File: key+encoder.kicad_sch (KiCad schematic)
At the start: 2 parts, among them SW10 SW_Push

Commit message: routing improvements
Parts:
- renumbered EN7 to EN5, SW10 to SW7
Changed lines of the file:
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@@
   (symbol (lib_id "Device:RotaryEncoder_Switch") (at 143.51 121.92 0) (mirror y)
     (in_bom yes) (on_board yes) (fields_autoplaced)
-    (property "Reference" "EN7" (id 0) (at 143.51 111.76 0))
+    (property "Reference" "EN5" (id 0) (at 143.51 111.76 0))
     (property "Value" "RotaryEncoder_Switch" (id 1) (at 143.51 114.3 0))
     (property "Footprint" "Keeby-Cat Footprints:RotaryEncoder_Alps_EC11E-Switch_Vertical_H20mm_nomount_alt" (id 2) (at 147.32 117.856 0)
@@
   (symbol (lib_id "Switch:SW_Push") (at 140.97 96.52 0)
     (in_bom yes) (on_board yes) (fields_autoplaced)
-    (property "Reference" "SW10" (id 0) (at 140.97 88.9 0))
+    (property "Reference" "SW7" (id 0) (at 140.97 88.9 0))
     (property "Value" "SW_Push" (id 1) (at 140.97 91.44 0))
     (property "Footprint" "kbd-footprints:CherryMX_1u_north" (id 2) (at 140.97 91.44 0)

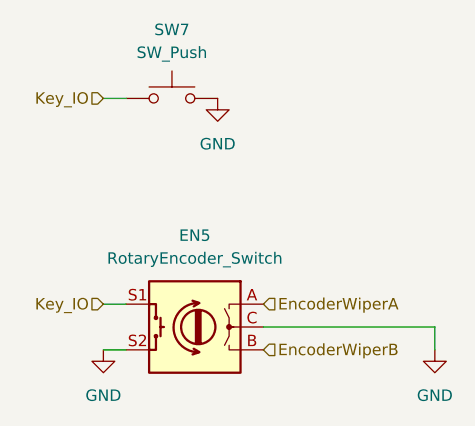
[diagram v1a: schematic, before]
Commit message: adjust schematic graphics
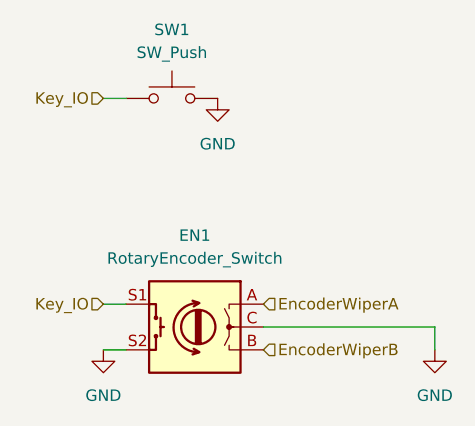
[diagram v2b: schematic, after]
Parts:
- renumbered EN5 to EN1, SW7 to SW1
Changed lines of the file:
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@@
     (effects (font (size 1.27 1.27)) (justify left))
   )
-  (symbol (lib_id "power:GND") (at 146.05 96.52 0)
+  (symbol (lib_id "power:GND") (at 146.05 96.52 0) (unit 1)
     (in_bom yes) (on_board yes) (fields_autoplaced)
-    (property "Reference" "#PWR020" (id 0) (at 146.05 102.87 0)
+    (property "Reference" "#PWR02" (id 0) (at 146.05 102.87 0)
       (effects (font (size 1.27 1.27)) hide)
     )
@@
     (pin "1")
   )
-  (symbol (lib_id "power:GND") (at 170.18 124.46 0)
+  (symbol (lib_id "power:GND") (at 170.18 124.46 0) (unit 1)
     (in_bom yes) (on_board yes) (fields_autoplaced)
-    (property "Reference" "#PWR021" (id 0) (at 170.18 130.81 0)
+    (property "Reference" "#PWR03" (id 0) (at 170.18 130.81 0)
       (effects (font (size 1.27 1.27)) hide)
     )
@@
     (pin "1")
   )
-  (symbol (lib_id "Device:RotaryEncoder_Switch") (at 143.51 121.92 0) (mirror y)
+  (symbol (lib_id "Device:RotaryEncoder_Switch") (at 143.51 121.92 0) (mirror y) (unit 1)
     (in_bom yes) (on_board yes) (fields_autoplaced)
-    (property "Reference" "EN5" (id 0) (at 143.51 111.76 0))
+    (property "Reference" "EN1" (id 0) (at 143.51 111.76 0))
     (property "Value" "RotaryEncoder_Switch" (id 1) (at 143.51 114.3 0))
     (property "Footprint" "Keeby-Cat Footprints:RotaryEncoder_Alps_EC11E-Switch_Vertical_H20mm_nomount_alt" (id 2) (at 147.32 117.856 0)
@@
     (pin "S2")
   )
-  (symbol (lib_id "power:GND") (at 133.35 124.46 0)
+  (symbol (lib_id "power:GND") (at 133.35 124.46 0) (unit 1)
     (in_bom yes) (on_board yes) (fields_autoplaced)
-    (property "Reference" "#PWR019" (id 0) (at 133.35 130.81 0)
+    (property "Reference" "#PWR01" (id 0) (at 133.35 130.81 0)
       (effects (font (size 1.27 1.27)) hide)
     )
@@
     (pin "1")
   )
-  (symbol (lib_id "Switch:SW_Push") (at 140.97 96.52 0)
+  (symbol (lib_id "Switch:SW_Push") (at 140.97 96.52 0) (unit 1)
     (in_bom yes) (on_board yes) (fields_autoplaced)
-    (property "Reference" "SW7" (id 0) (at 140.97 88.9 0))
+    (property "Reference" "SW1" (id 0) (at 140.97 88.9 0))
     (property "Value" "SW_Push" (id 1) (at 140.97 91.44 0))
     (property "Footprint" "kbd-footprints:CherryMX_1u_north" (id 2) (at 140.97 91.44 0)
